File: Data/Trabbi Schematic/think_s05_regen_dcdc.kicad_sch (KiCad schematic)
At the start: 4 parts, among them U1 DC/DC Converter (E07), U2 HV Distribution Box

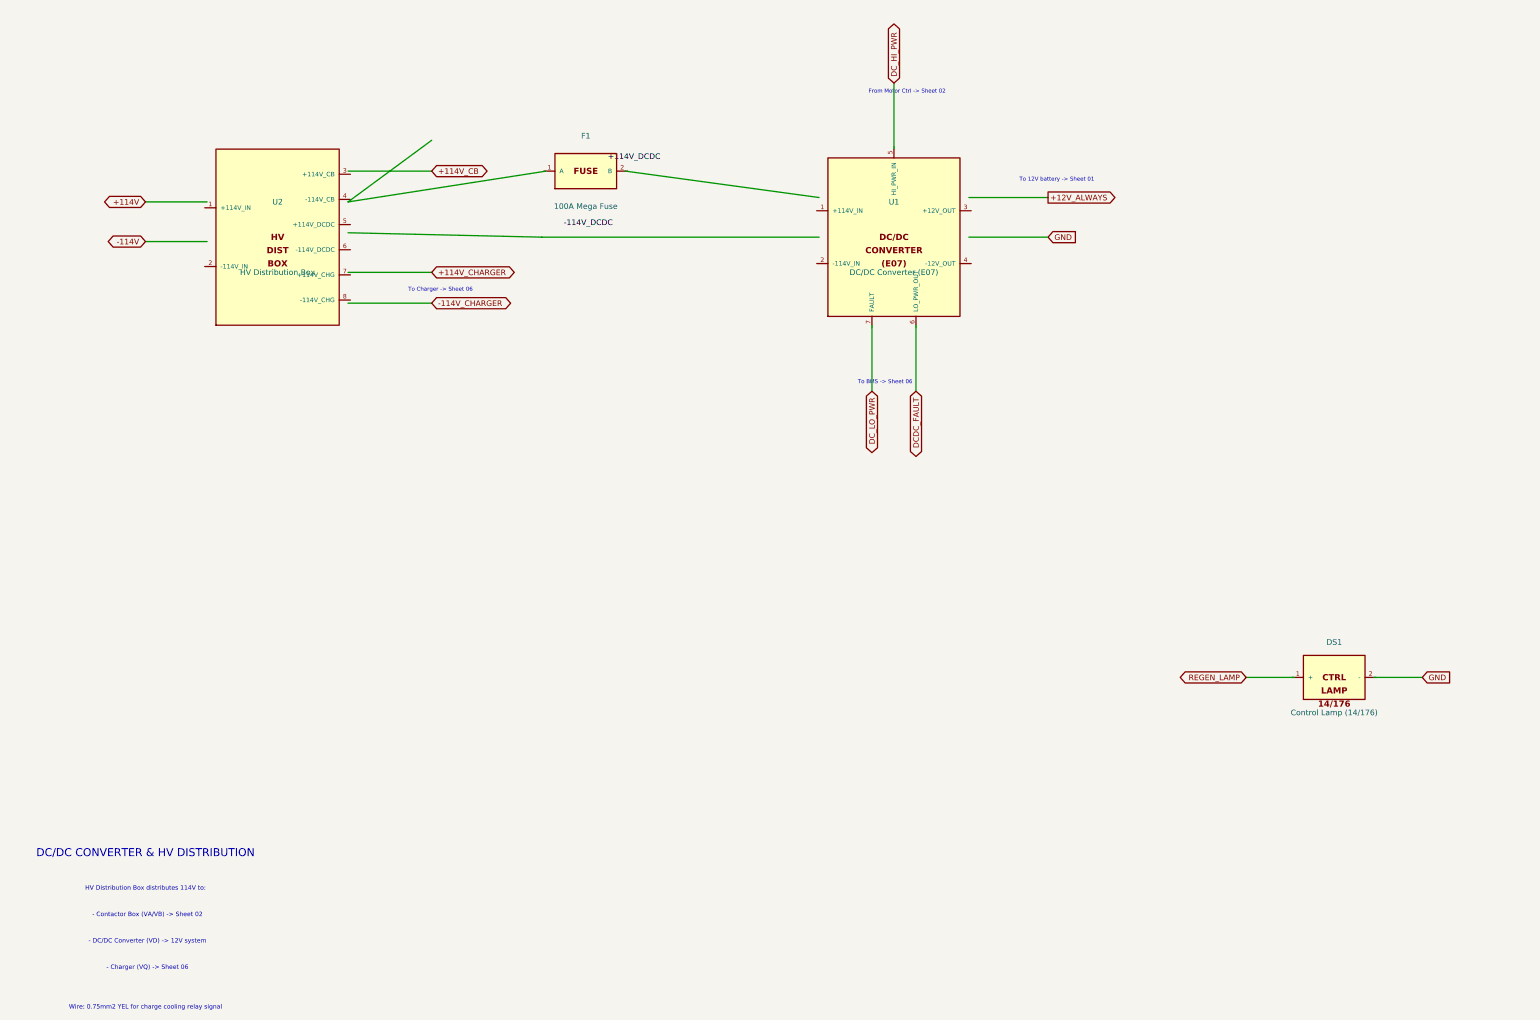
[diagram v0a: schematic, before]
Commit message: Fix wire-to-pin connections: use exact calculated pin positions
Refactored gen_think_complete.py to compute exact pin schematic
coordinates instead of using approximate manual offsets. Added p()
method to Sheet class that transforms symbol-local pin positions to
schematic coordinates. All 232 wire calls across 13 sub-sheet
generators now use p() for pin endpoints, fixing misaligned
connections (previously off by 0.54-10+ units).

Co-Authored-By: Claude Opus 4.6 <noreply@anthropic.com>
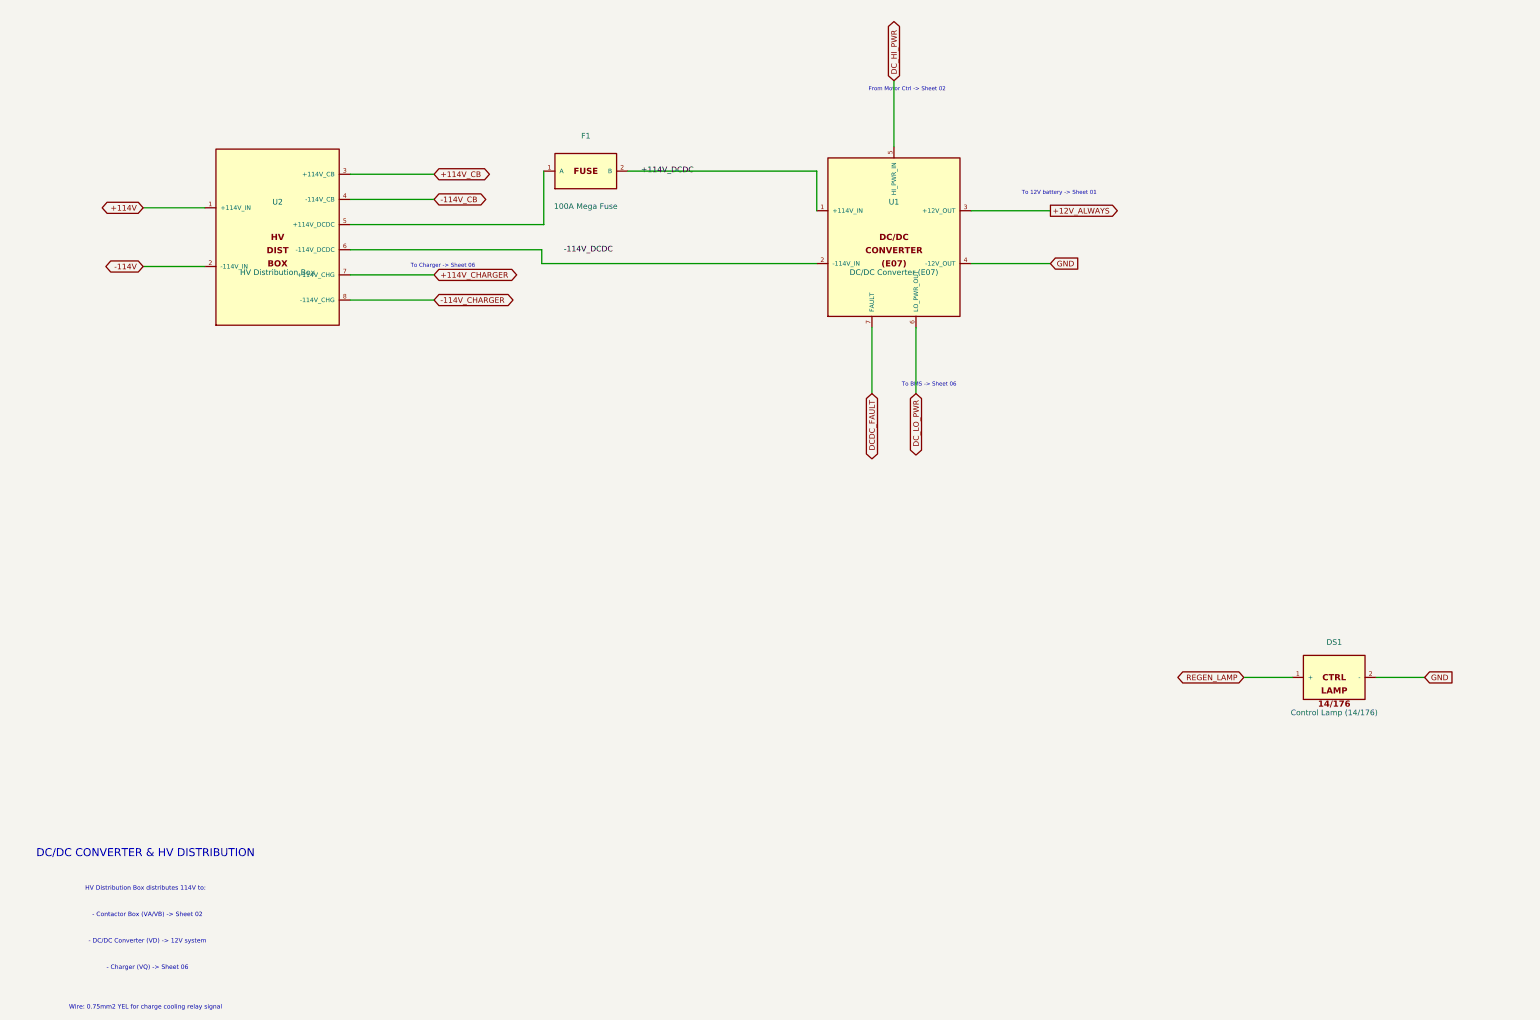
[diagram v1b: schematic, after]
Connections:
- net +114V: now also U2.1 (+114V_IN)
- net +114V_CB: now also U2.3 (+114V_CB)
- net +114V_CHARGER: now also U2.7 (+114V_CHG)
- net +114V_DCDC: now also F1.2 (B), U1.1 (+114V_IN)
- net +12V_ALWAYS: now also U1.3 (+12V_OUT)
- net -114V: now also U2.2 (-114V_IN)
- net -114V_CHARGER: now also U2.8 (-114V_CHG)
- net DCDC_FAULT: now also U1.7 (FAULT)
- net DC_HI_PWR: now also U1.5 (HI_PWR_IN)
- net DC_LO_PWR: now also U1.6 (LO_PWR_OUT)
- net GND: now also DS1.2 (-), U1.4 (-12V_OUT)
- net REGEN_LAMP: now also DS1.1 (+)
- net -114V_CB: now reaches U2.4 (-114V_CB)
- net at U2.5 (+114V_DCDC): now also F1.1 (A)
- net at U2.6 (-114V_DCDC): now also U1.2 (-114V_IN)
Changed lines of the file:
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@@
     (pin "2")
   )
-  (wire (pts (xy 76.000 92.000) (xy 121.000 85.000))
+  (wire (pts (xy 76.540 97.143) (xy 120.460 97.143))
     (stroke (width 0) (type default))
   )
-  (wire (pts (xy 139.000 85.000) (xy 183.000 91.000))
+  (wire (pts (xy 120.460 97.143) (xy 120.460 85.000))
     (stroke (width 0) (type default))
   )
-  (label "+114V_DCDC" (at 135.000 82.000 0)
+  (wire (pts (xy 139.540 85.000) (xy 182.460 85.000))
+    (stroke (width 0) (type default))
+  )
+  (wire (pts (xy 182.460 85.000) (xy 182.460 94.000))
+    (stroke (width 0) (type default))
+  )
+  (label "+114V_DCDC" (at 142.540 85.000 0)
     (effects (font (size 1.27 1.27)))
   )
-  (wire (pts (xy 76.000 99.000) (xy 120.000 100.000))
+  (wire (pts (xy 76.540 102.857) (xy 120.000 102.857))
     (stroke (width 0) (type default))
   )
-  (wire (pts (xy 120.000 100.000) (xy 183.000 100.000))
+  (wire (pts (xy 120.000 102.857) (xy 120.000 106.000))
     (stroke (width 0) (type default))
   )
-  (label "-114V_DCDC" (at 125.000 97.000 0)
+  (wire (pts (xy 120.000 106.000) (xy 182.460 106.000))
+    (stroke (width 0) (type default))
+  )
+  (label "-114V_DCDC" (at 125.000 103.000 0)
     (effects (font (size 1.27 1.27)))
   )
-  (wire (pts (xy 217.000 91.000) (xy 235.000 91.000))
+  (wire (pts (xy 217.540 94.000) (xy 235.540 94.000))
     (stroke (width 0) (type default))
   )
-  (global_label "+12V_ALWAYS" (shape output) (at 235.000 91.000 0)
+  (global_label "+12V_ALWAYS" (shape output) (at 235.540 94.000 0)
     (effects (font (size 1.27 1.27)))
-    (property "Intersheetrefs" "${INTERSHEET_REFS}" (at 235.000 91.000 0)
+    (property "Intersheetrefs" "${INTERSHEET_REFS}" (at 235.540 94.000 0)
       (effects (font (size 1.27 1.27)) hide)
     )
   )
-  (text "To 12V battery -> Sheet 01" (at 237.000 87.000 0)
+  (text "To 12V battery -> Sheet 01" (at 237.540 90.000 0)
     (effects (font (size 0.900 0.900)))
   )
-  (wire (pts (xy 217.000 100.000) (xy 235.000 100.000))
+  (wire (pts (xy 217.540 106.000) (xy 235.540 106.000))
     (stroke (width 0) (type default))
   )
-  (global_label "GND" (shape input) (at 235.000 100.000 0)
+  (global_label "GND" (shape input) (at 235.540 106.000 0)
     (effects (font (size 1.27 1.27)))
-    (property "Intersheetrefs" "${INTERSHEET_REFS}" (at 235.000 100.000 0)
+    (property "Intersheetrefs" "${INTERSHEET_REFS}" (at 235.540 106.000 0)
       (effects (font (size 1.27 1.27)) hide)
     )
   )
-  (wire (pts (xy 200.000 80.000) (xy 200.000 65.000))
+  (wire (pts (xy 200.000 79.460) (xy 200.000 64.460))
     (stroke (width 0) (type default))
   )
-  (global_label "DC_HI_PWR" (shape bidirectional) (at 200.000 65.000 90)
+  (global_label "DC_HI_PWR" (shape bidirectional) (at 200.000 64.460 90)
     (effects (font (size 1.27 1.27)))
-    (property "Intersheetrefs" "${INTERSHEET_REFS}" (at 200.000 65.000 0)
+    (property "Intersheetrefs" "${INTERSHEET_REFS}" (at 200.000 64.460 0)
       (effects (font (size 1.27 1.27)) hide)
     )
   )
-  (text "From Motor Ctrl -> Sheet 02" (at 203.000 67.000 0)
+  (text "From Motor Ctrl -> Sheet 02" (at 203.000 66.460 0)
     (effects (font (size 0.900 0.900)))
   )
-  (wire (pts (xy 195.000 120.000) (xy 195.000 135.000))
+  (wire (pts (xy 205.000 120.540) (xy 205.000 135.540))
     (stroke (width 0) (type default))
   )
-  (global_label "DC_LO_PWR" (shape bidirectional) (at 195.000 135.000 270)
+  (global_label "DC_LO_PWR" (shape bidirectional) (at 205.000 135.540 270)
     (effects (font (size 1.27 1.27)))
-    (property "Intersheetrefs" "${INTERSHEET_REFS}" (at 195.000 135.000 0)
+    (property "Intersheetrefs" "${INTERSHEET_REFS}" (at 205.000 135.540 0)
       (effects (font (size 1.27 1.27)) hide)
     )
   )
-  (text "To BMS -> Sheet 06" (at 198.000 133.000 0)
+  (text "To BMS -> Sheet 06" (at 208.000 133.540 0)
     (effects (font (size 0.900 0.900)))
   )
-  (wire (pts (xy 205.000 120.000) (xy 205.000 135.000))
+  (wire (pts (xy 195.000 120.540) (xy 195.000 135.540))
     (stroke (width 0) (type default))
   )
-  (global_label "DCDC_FAULT" (shape bidirectional) (at 205.000 135.000 270)
+  (global_label "DCDC_FAULT" (shape bidirectional) (at 195.000 135.540 270)
     (effects (font (size 1.27 1.27)))
-    (property "Intersheetrefs" "${INTERSHEET_REFS}" (at 205.000 135.000 0)
+    (property "Intersheetrefs" "${INTERSHEET_REFS}" (at 195.000 135.540 0)
       (effects (font (size 1.27 1.27)) hide)
     )
   )
-  (wire (pts (xy 44.000 92.000) (xy 30.000 92.000))
+  (wire (pts (xy 43.460 93.333) (xy 29.460 93.333))
     (stroke (width 0) (type default))
   )
-  (global_label "+114V" (shape bidirectional) (at 30.000 92.000 180)
+  (global_label "+114V" (shape bidirectional) (at 29.460 93.333 180)
     (effects (font (size 1.27 1.27)))
-    (property "Intersheetrefs" "${INTERSHEET_REFS}" (at 30.000 92.000 0)
+    (property "Intersheetrefs" "${INTERSHEET_REFS}" (at 29.460 93.333 0)
       (effects (font (size 1.27 1.27)) hide)
     )
   )
-  (wire (pts (xy 44.000 101.000) (xy 30.000 101.000))
+  (wire (pts (xy 43.460 106.667) (xy 29.460 106.667))
     (stroke (width 0) (type default))
   )
-  (global_label "-114V" (shape bidirectional) (at 30.000 101.000 180)
+  (global_label "-114V" (shape bidirectional) (at 29.460 106.667 180)
     (effects (font (size 1.27 1.27)))
-    (property "Intersheetrefs" "${INTERSHEET_REFS}" (at 30.000 101.000 0)
+    (property "Intersheetrefs" "${INTERSHEET_REFS}" (at 29.460 106.667 0)
       (effects (font (size 1.27 1.27)) hide)
     )
   )
-  (wire (pts (xy 76.000 85.000) (xy 95.000 85.000))
+  (wire (pts (xy 76.540 85.714) (xy 95.540 85.714))
     (stroke (width 0) (type default))
   )
-  (global_label "+114V_CB" (shape bidirectional) (at 95.000 85.000 0)
+  (global_label "+114V_CB" (shape bidirectional) (at 95.540 85.714 0)
     (effects (font (size 1.27 1.27)))
-    (property "Intersheetrefs" "${INTERSHEET_REFS}" (at 95.000 85.000 0)
+    (property "Intersheetrefs" "${INTERSHEET_REFS}" (at 95.540 85.714 0)
       (effects (font (size 1.27 1.27)) hide)
     )
   )
-  (wire (pts (xy 76.000 92.000) (xy 95.000 78.000))
+  (wire (pts (xy 76.540 91.429) (xy 95.540 91.429))
     (stroke (width 0) (type default))
   )
-  (wire (pts (xy 76.000 108.000) (xy 95.000 108.000))
-    (stroke (width 0) (type default))
-  )
-  (global_label "+114V_CHARGER" (shape bidirectional) (at 95.000 108.000 0)
+  (global_label "-114V_CB" (shape bidirectional) (at 95.540 91.429 0)
     (effects (font (size 1.27 1.27)))
-    (property "Intersheetrefs" "${INTERSHEET_REFS}" (at 95.000 108.000 0)
+    (property "Intersheetrefs" "${INTERSHEET_REFS}" (at 95.540 91.429 0)
       (effects (font (size 1.27 1.27)) hide)
     )
   )
-  (wire (pts (xy 76.000 115.000) (xy 95.000 115.000))
+  (wire (pts (xy 76.540 108.571) (xy 95.540 108.571))
     (stroke (width 0) (type default))
   )
-  (global_label "-114V_CHARGER" (shape bidirectional) (at 95.000 115.000 0)
+  (global_label "+114V_CHARGER" (shape bidirectional) (at 95.540 108.571 0)
     (effects (font (size 1.27 1.27)))
-    (property "Intersheetrefs" "${INTERSHEET_REFS}" (at 95.000 115.000 0)
+    (property "Intersheetrefs" "${INTERSHEET_REFS}" (at 95.540 108.571 0)
       (effects (font (size 1.27 1.27)) hide)
     )
   )
-  (text "To Charger -> Sheet 06" (at 97.000 112.000 0)
-    (effects (font (size 0.900 0.900)))
-  )
-  (wire (pts (xy 291.000 200.000) (xy 280.000 200.000))
+  (wire (pts (xy 76.540 114.286) (xy 95.540 114.286))
     (stroke (width 0) (type default))
   )
-  (global_label "REGEN_LAMP" (shape bidirectional) (at 280.000 200.000 180)
+  (global_label "-114V_CHARGER" (shape bidirectional) (at 95.540 114.286 0)
     (effects (font (size 1.27 1.27)))
-    (property "Intersheetrefs" "${INTERSHEET_REFS}" (at 280.000 200.000 0)
+    (property "Intersheetrefs" "${INTERSHEET_REFS}" (at 95.540 114.286 0)
       (effects (font (size 1.27 1.27)) hide)
     )
   )
-  (wire (pts (xy 309.000 200.000) (xy 320.000 200.000))
+  (text "To Charger -> Sheet 06" (at 97.540 106.571 0)
+    (effects (font (size 0.900 0.900)))
+  )
+  (wire (pts (xy 290.460 200.000) (xy 279.460 200.000))
     (stroke (width 0) (type default))
   )
-  (global_label "GND" (shape input) (at 320.000 200.000 0)
+  (global_label "REGEN_LAMP" (shape bidirectional) (at 279.460 200.000 180)
     (effects (font (size 1.27 1.27)))
-    (property "Intersheetrefs" "${INTERSHEET_REFS}" (at 320.000 200.000 0)
+    (property "Intersheetrefs" "${INTERSHEET_REFS}" (at 279.460 200.000 0)
       (effects (font (size 1.27 1.27)) hide)
     )
+  )
+  (wire (pts (xy 309.540 200.000) (xy 320.540 200.000))
+    (stroke (width 0) (type default))
+  )
+  (global_label "GND" (shape input) (at 320.540 200.000 0)
+    (effects (font (size 1.27 1.27)))
+    (property "Intersheetrefs" "${INTERSHEET_REFS}" (at 320.540 200.000 0)
+      (effects (font (size 1.27 1.27)) hide)
+    )

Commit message: Enforce orthogonal routing and 1.27mm grid alignment
- Add _g() grid snap function to Sheet class (rounds all coordinates to nearest 1.27mm)
- Add wire_l() method for L-shaped orthogonal routing (horizontal+vertical segments)
- Apply grid snapping in p(), place(), wire(), label(), glabel(), junction(), no_connect(), defsym()
- Replace all 19 diagonal wire calls with wire_l() across S02, S06, S07, S08, S10, S12, S13
- All wire segments now strictly horizontal or vertical, no diagonals
- All coordinates verified on 1.27mm (50mil) KiCad standard grid

Co-Authored-By: Claude Opus 4.6 <noreply@anthropic.com>
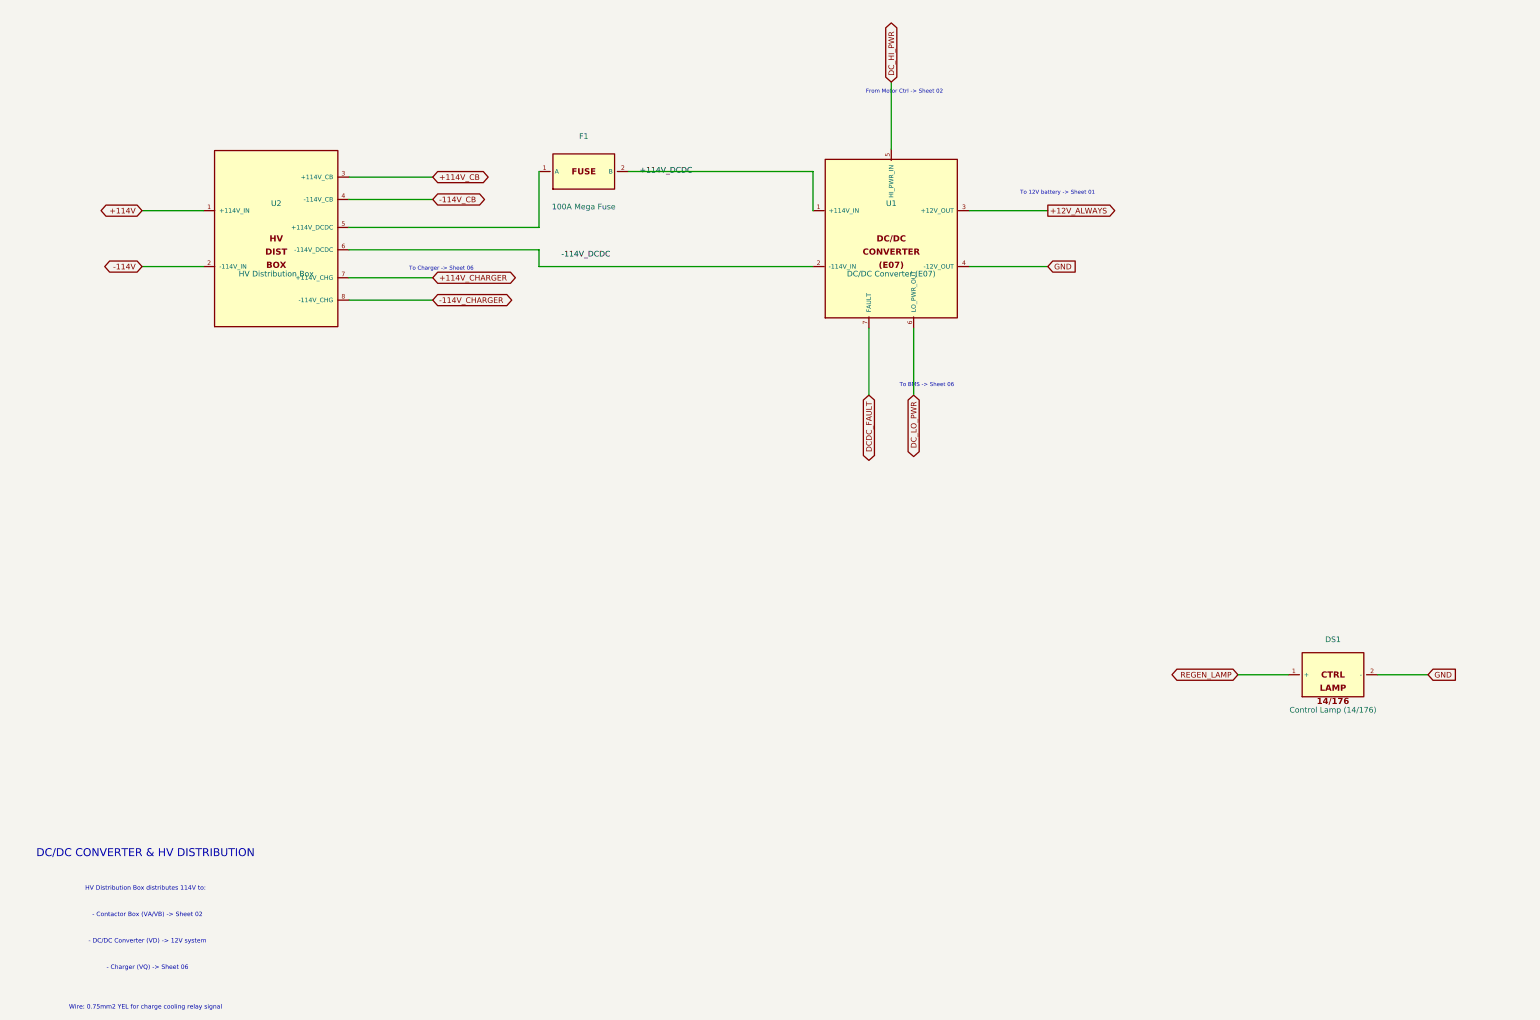
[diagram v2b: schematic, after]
